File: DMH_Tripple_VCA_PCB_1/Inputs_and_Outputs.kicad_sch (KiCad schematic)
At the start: 33 parts, among them J0 Conn_01x01, J1 TS_Jack_6.35mm_Sw, J10 TS_Jack_6.35mm_Sw, J2 TS_Jack_6.35mm_Sw, J200 IDC_02x05, J3 TS_Jack_6.35mm_Sw, J4 TS_Jack_6.35mm_Sw, J5 TS_Jack_6.35mm_Sw, J50 Conn_01x06, J6 TS_Jack_6.35mm_Sw, J60 Conn_01x06, J7 TS_Jack_6.35mm_Sw, J70 Conn_01x06, J8 TS_Jack_6.35mm_Sw, J9 TS_Jack_6.35mm_Sw, SW1 SW_DPDT, SW2 SW_DPDT, SW3 SW_DPDT

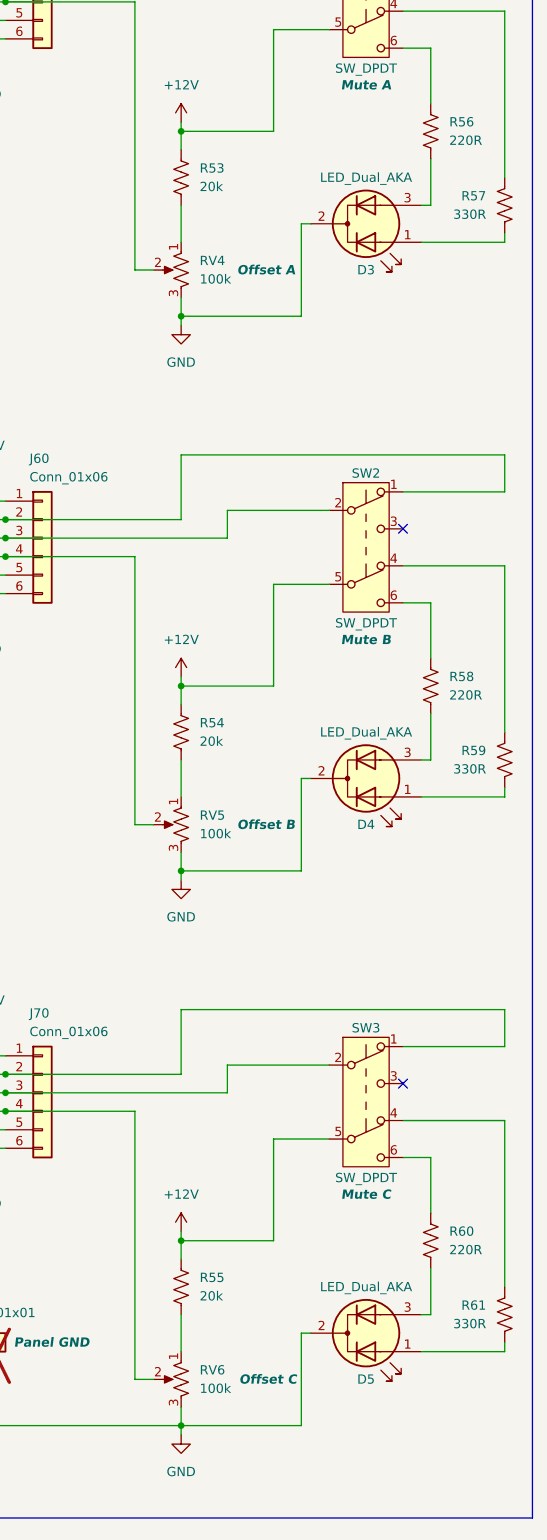
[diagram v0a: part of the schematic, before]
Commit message: Fixed mistakes in PCB 2
- Inverted offset potentiometers pinout
- LED resistors were too low, changed to 1k both colors
- Regenerated PCB 2 gerbers accordingly
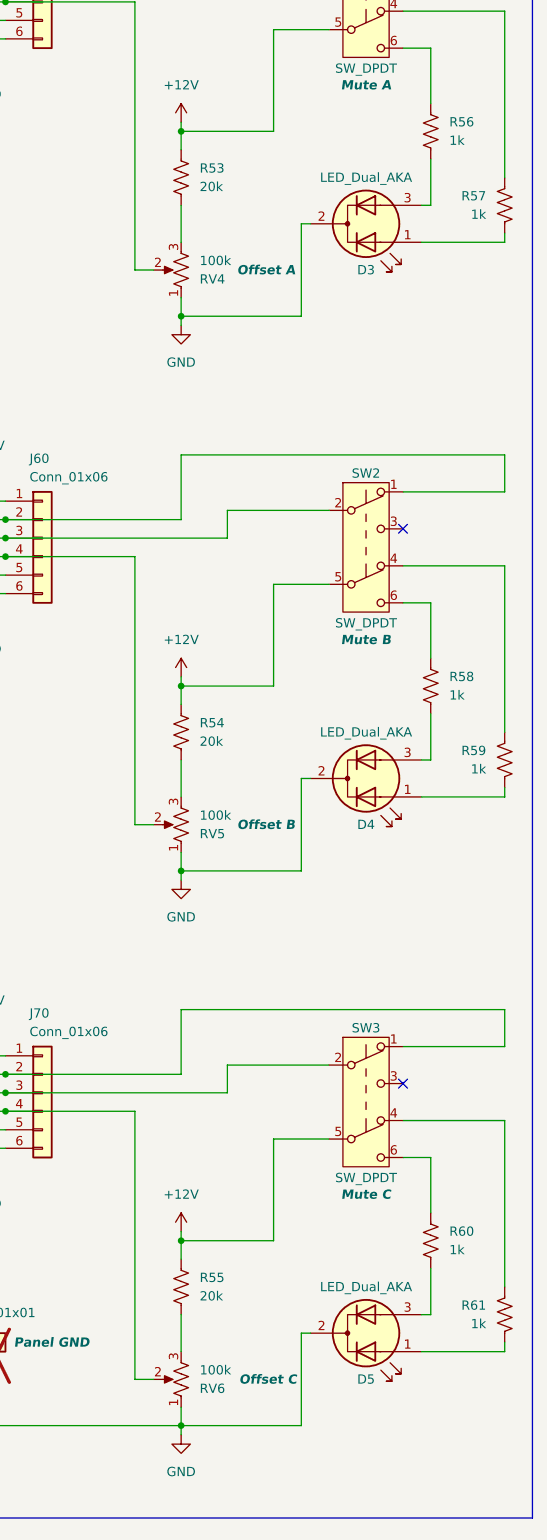
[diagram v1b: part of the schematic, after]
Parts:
- R56, R58, R60: value 220R -> 1k
- R57, R59, R61: value 330R -> 1k
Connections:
- net GND: now also RV4.1, RV5.1, RV6.1; no longer RV4.3, RV5.3, RV6.3
- net at R54.1: now also RV5.3; no longer RV5.1
- net at R53.1: now also RV4.3; no longer RV4.1
- net at R55.1: now also RV6.3; no longer RV6.1
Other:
- moved on the sheet: RV4, RV5, RV6
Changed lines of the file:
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@@
 			)
 		)
-		(property "Value" "220R"
+		(property "Value" "1k"
 			(at 182.88 58.4199 0)
 			(effects
@@
 	(symbol
 		(lib_id "Device:R_Potentiometer_US")
-		(at 146.05 152.4 0)
-		(mirror y)
+		(at 146.05 152.4 180)
 		(unit 1)
 		(exclude_from_sim no)
@@
 		(dnp no)
 		(property "Reference" "RV5"
-			(at 148.59 151.1299 0)
+			(at 148.59 153.6701 0)
 			(effects
 				(font
@@
 		)
 		(property "Value" "100k"
-			(at 148.59 153.6699 0)
+			(at 148.59 151.1301 0)
 			(effects
 				(font
@@
 			)
 		)
-		(property "Value" "220R"
+		(property "Value" "1k"
 			(at 182.88 210.8199 0)
 			(effects
@@
 	(symbol
 		(lib_id "Device:R_Potentiometer_US")
-		(at 146.05 76.2 0)
-		(mirror y)
+		(at 146.05 76.2 180)
 		(unit 1)
 		(exclude_from_sim no)
@@
 		(dnp no)
 		(property "Reference" "RV4"
-			(at 148.59 74.9299 0)
+			(at 148.59 77.4701 0)
 			(effects
 				(font
@@
 		)
 		(property "Value" "100k"
-			(at 148.59 77.4699 0)
+			(at 148.59 74.9301 0)
 			(effects
 				(font
@@
 			)
 		)
-		(property "Value" "220R"
+		(property "Value" "1k"
 			(at 182.88 134.6199 0)
 			(effects
@@
 			)
 		)
-		(property "Value" "330R"
+		(property "Value" "1k"
 			(at 187.96 220.9799 0)
 			(effects
@@
 	(symbol
 		(lib_id "Device:R_Potentiometer_US")
-		(at 146.05 228.6 0)
-		(mirror y)
+		(at 146.05 228.6 180)
 		(unit 1)
 		(exclude_from_sim no)
@@
 		(dnp no)
 		(property "Reference" "RV6"
-			(at 148.59 227.3299 0)
+			(at 148.59 229.8701 0)
 			(effects
 				(font
@@
 		)
 		(property "Value" "100k"
-			(at 148.59 229.8699 0)
+			(at 148.59 227.3301 0)
 			(effects
 				(font
@@
 			)
 		)
-		(property "Value" "330R"
+		(property "Value" "1k"
 			(at 187.96 68.5799 0)
 			(effects
@@
 			)
 		)
-		(property "Value" "330R"
+		(property "Value" "1k"
 			(at 187.96 144.7799 0)
 			(effects
